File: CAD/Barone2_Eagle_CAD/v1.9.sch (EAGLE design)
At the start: 57 parts, among them J1 USB_C_Port_Raspberry_Pi, J2 XT60-M, J3 10033854-052FSLF, M1 PIC32MX340F512H-80I/MR, M2 RaspberryPi_DDR2_SODIMM_1.8V, Q2 BSS138

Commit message: wiring up board
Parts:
- removed 2V8_OUT: STMICROELECTRONICS_LD1117DT33CTRSTMICROELECTRONICS_LD1117DT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, STMicroelectronics - LD1117DT33CTR:STMICROELECTRONICS_LD1117DT33CTRSTMICROELECTRONICS_LD1117DT33CTR_0_2
- removed C10: 0.1uF, rcl:C-USC0805
- removed C8: 10uF, rcl:C-USC0805
- removed J3: 10033854-052FSLF, 10033854-052FSLF:10033854-052FSLF
- removed M2: RaspberryPi_DDR2_SODIMM_1.8V, con-amp:1376408-SLOT_1.8V
- added 1V8_OUT1: STMICROELECTRONICS_LD1117DT33CTRSTMICROELECTRONICS_LD1117DT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, STMicroelectronics - LD1117DT33CTR:STMICROELECTRONICS_LD1117DT33CTRSTMICROELECTRONICS_LD1117DT33CTR_0_2
- added C20: 10uF, rcl:C-USC0805
- added C21: 0.1uF, rcl:C-USC0805
- added C22: 0.01uF, rcl:C-USC0805
- added JP1: (no value), adafruit:PINHD-1X8CLEANBIG
- added Q1, SCL_OUT_IMU1: BSS138, BSS138:BSS138
- added SODIMM_M2_PINOUT: 10033854-052FSLF, 10033854-052FSLF:10033854-052FSLF
- added X1: CB3LV-3C-8M0000, CB3LV-3C-20M0000:CB3LV-3C-20M0000
- added Y1: ABRACON_ASEK-32_768KHZ-LRTABRACON_ASEK-32_768KHZ-LRT_0_0, Abracon - ASEK-32.768KHZ-LRT:ABRACON_ASEK-32_768KHZ-LRTABRACON_ASEK-32_768KHZ-LRT_0_0
- SON_0: SPICEPREFIX (none) -> X
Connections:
- net +5V renamed 5V
- net N$1 renamed VCAP_VCORE_M1
- removed net 2.8V: 2V8_OUT.VOUT, C8.1
- removed net D+_M2: J1.D-, M2-167.1
- removed net D-_M2: J1.D+, M2-165.1
- removed net M2_1V8: M2-183.1, M2-184.1, M2-185.1, M2-186.1
- removed net M2_VBAT: M2-197.1, M2-198.1, M2-199.1, M2-200.1
- removed net MISO_M1: M1.AN4/C1IN-/CN6/RB4, M2-29.1, R1.2, U$6.DATA_OUT
- removed net MOSI_M1: M1.AN5/C1IN+/CN7/RB5, M2-33.1, R11.2, U$6.DATA_IN
- removed net N$15: M2-41.1, M2-42.1
- removed net SCK_M1: M1.AN3/C2IN+/CN5/RB3, M2-35.1, R12.2, U$6.SCLK
- new net AVDD3_M1: C16.2, M1.VDD3
- new net AVDD_M1: C5.2, M1.AVDD
- new net AVSS_M1: C5.1, M1.AVSS
- new net GPIO13_M2: JP1.8, SODIMM_M2_PINOUTG$1.47
- new net GPIO14_M2: JP1.7, SODIMM_M2_PINOUTG$1.51
- new net GPIO15_M2: JP1.6, SODIMM_M2_PINOUTG$1.53
- new net GPIO16_M2: JP1.5, SODIMM_M2_PINOUTG$1.57
- new net GPIO17_M2: JP1.4, SODIMM_M2_PINOUTG$1.59
- new net GPIO18_M2: JP1.3, SODIMM_M2_PINOUTG$1.63
- new net GPIO19_M2: JP1.2, SODIMM_M2_PINOUTG$1.65
- new net GPIO20_M2: JP1.1, SODIMM_M2_PINOUTG$1.69
- new net IMU_SDA: IMU.SDA/SDI, Q1.D, SCL_OUT_IMU1.G
- new net MISO_M2: M1.AN4/C1IN-/CN6/RB4, R1.2, SODIMM_M2_PINOUTG$1.29, U$6.DATA_OUT
- new net MOSI_M2: M1.AN5/C1IN+/CN7/RB5, R11.2, SODIMM_M2_PINOUTG$1.33, U$6.DATA_IN
- new net N$1: GPS.VCC
- new net N$4: R7.2
- new net N$6: M1.OSC2/CLKO/RC15, X1.EOH
- new net N$7: M1.OSC1/CLKI/RC12, X1.OUT
- new net N$8: M1.SOSCO/T1CK/CN0/RC14, Y1.TRI-STATE
- new net SCK_M2: M1.AN3/C2IN+/CN5/RB3, R12.2, SODIMM_M2_PINOUTG$1.35, U$6.SCLK
- new net USB_D+_M2: J1.D+, SODIMM_M2_PINOUTG$2.165
- new net USB_D-_M2: J1.D-, SODIMM_M2_PINOUTG$2.167
- new net VDD1_M1: C17.2, M1.VDD1
- new net VSS1_M1: C17.1, M1.VSS1
- new net VSS3_M1: C16.1, M1.VSS3
- net 1.8V: now also 1V8_OUT1.VOUT, C14.1, C20.1, IMU.VDD, IMU.VDDIO, Q1.S, Q2.S, SODIMM_M2_PINOUTG$2.183, SODIMM_M2_PINOUTG$2.184, SODIMM_M2_PINOUTG$2.185, SODIMM_M2_PINOUTG$2.186
- net 9.6V-12.6V: no longer 1V8_OUT.VIN, 2V8_OUT.VIN, 5V_OUT.VIN, C10.1, C4.1, C9.1
- net CS_M1: now also SODIMM_M2_PINOUTG$1.4, SODIMM_M2_PINOUTG$1.5; no longer J3G$1.5, M2-5.1
- net CS_MICRO_SD: now also SODIMM_M2_PINOUTG$1.2; no longer J3G$1.2, M2-3.1
- net GND: now also 1V8_OUT1.GND, C20.2, C21.2, C22.2, SODIMM_M2_PINOUTG$1.19, SODIMM_M2_PINOUTG$1.20, SODIMM_M2_PINOUTG$1.31, SODIMM_M2_PINOUTG$1.32, SODIMM_M2_PINOUTG$1.37, SODIMM_M2_PINOUTG$1.38, SODIMM_M2_PINOUTG$1.43, SODIMM_M2_PINOUTG$1.44, SODIMM_M2_PINOUTG$1.49, SODIMM_M2_PINOUTG$1.50, SODIMM_M2_PINOUTG$1.55, SODIMM_M2_PINOUTG$1.56, SODIMM_M2_PINOUTG$1.61, SODIMM_M2_PINOUTG$1.62, SODIMM_M2_PINOUTG$1.67, SODIMM_M2_PINOUTG$1.68, SODIMM_M2_PINOUTG$1.7, SODIMM_M2_PINOUTG$1.73, SODIMM_M2_PINOUTG$1.74, SODIMM_M2_PINOUTG$1.79, SODIMM_M2_PINOUTG$1.8, SODIMM_M2_PINOUTG$1.80, SODIMM_M2_PINOUTG$1.85, SODIMM_M2_PINOUTG$1.86, SODIMM_M2_PINOUTG$1.91, SODIMM_M2_PINOUTG$1.92, SODIMM_M2_PINOUTG$1.97, SODIMM_M2_PINOUTG$1.98, SODIMM_M2_PINOUTG$1.SHIELD, SODIMM_M2_PINOUTG$2.103, SODIMM_M2_PINOUTG$2.104, SODIMM_M2_PINOUTG$2.109, SODIMM_M2_PINOUTG$2.110, SODIMM_M2_PINOUTG$2.115, SODIMM_M2_PINOUTG$2.116, SODIMM_M2_PINOUTG$2.121, SODIMM_M2_PINOUTG$2.122, SODIMM_M2_PINOUTG$2.127, SODIMM_M2_PINOUTG$2.133, SODIMM_M2_PINOUTG$2.134, SODIMM_M2_PINOUTG$2.139, SODIMM_M2_PINOUTG$2.140, SODIMM_M2_PINOUTG$2.145, SODIMM_M2_PINOUTG$2.146, SODIMM_M2_PINOUTG$2.151, SODIMM_M2_PINOUTG$2.152, SODIMM_M2_PINOUTG$2.157, SODIMM_M2_PINOUTG$2.163, SODIMM_M2_PINOUTG$2.164, SODIMM_M2_PINOUTG$2.168, SODIMM_M2_PINOUTG$2.169, SODIMM_M2_PINOUTG$2.170, SODIMM_M2_PINOUTG$2.181, SODIMM_M2_PINOUTG$2.182, SODIMM_M2_PINOUTG$2.187, SODIMM_M2_PINOUTG$2.188, SODIMM_M2_PINOUTG$2.195, SODIMM_M2_PINOUTG$2.196, X1.GND, Y1.GND; no longer 2V8_OUT.GND, C10.2, C16.1, C17.1, C5.1, C8.2, J3G$1.7, J3G$1.8, M1.AVSS, M1.VSS1, M1.VSS3, M2-1.1, M2-103.1, M2-104.1, M2-109.1, M2-110.1, M2-115.1, M2-116.1, M2-121.1, M2-122.1, M2-127.1, M2-13.1, M2-133.1, M2-134.1, M2-139.1, M2-14.1, M2-140.1, M2-145.1, M2-146.1, M2-151.1, M2-152.1, M2-157.1, M2-163.1, M2-164.1, M2-168.1, M2-169.1, M2-170.1, M2-181.1, M2-182.1, M2-187.1, M2-188.1, M2-19.1, M2-195.1, M2-196.1, M2-20.1, M2-25.1, M2-26.1, M2-31.1, M2-32.1, M2-37.1, M2-38.1, M2-43.1, M2-44.1, M2-49.1, M2-50.1, M2-55.1, M2-56.1, M2-61.1, M2-62.1, M2-67.1, M2-68.1, M2-7.1, M2-73.1, M2-74.1, M2-79.1, M2-8.1, M2-80.1, M2-85.1, M2-86.1, M2-91.1, M2-92.1, M2-97.1, M2-98.1
- net GPIO12_M2: now also SODIMM_M2_PINOUTG$1.45; no longer M2-45.1
- net GPIO2_M2: now also SODIMM_M2_PINOUTG$1.9; no longer M2-9.1
- net GPIO3_M2: now also SODIMM_M2_PINOUTG$1.11; no longer M2-11.1
- net GPIO4_M2: now also SODIMM_M2_PINOUTG$1.15; no longer M2-15.1
- net GPIO5_M2: now also SODIMM_M2_PINOUTG$1.17; no longer M2-17.1
- net GPIO6_M2: now also SODIMM_M2_PINOUTG$1.21; no longer M2-21.1
- net GPIO7_M2: now also SODIMM_M2_PINOUTG$1.23; no longer M2-23.1
- net GPIO8_M2: now also SODIMM_M2_PINOUTG$1.27; no longer M2-27.1
- net N$9: now also M1.SOSCI/CN1/RC13, Y1.OUTPUT; no longer M2-39.1, M2-40.1
- net SDA_M1: now also Q1.G, SCL_OUT_IMU1.D; no longer IMU.SDA/SDI
- net VIN: now also 1V8_OUT.VIN, 1V8_OUT1.VIN, 5V_OUT.VIN, C21.1, C22.1, C4.1, C9.1, SCL_OUT_IMU1.S, SODIMM_M2_PINOUTG$1.39, SODIMM_M2_PINOUTG$1.40, SODIMM_M2_PINOUTG$1.41, SODIMM_M2_PINOUTG$1.42, SODIMM_M2_PINOUTG$2.189, SODIMM_M2_PINOUTG$2.190, SODIMM_M2_PINOUTG$2.191, SODIMM_M2_PINOUTG$2.192, SODIMM_M2_PINOUTG$2.193, SODIMM_M2_PINOUTG$2.194, SODIMM_M2_PINOUTG$2.197, SODIMM_M2_PINOUTG$2.198, SODIMM_M2_PINOUTG$2.199, SODIMM_M2_PINOUTG$2.200, X1.VCC, Y1.VDD; no longer C14.1, C16.2, C17.2, C5.2, GPS.VCC, IMU.VDD, IMU.VDDIO, M1.AVDD, M1.VDD1, M1.VDD3, M2-189.1, M2-190.1, M2-191.1, M2-193.1, Q2.S, R7.2
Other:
- note added: "(PIN168)USB_OTGID connected to GND when unused"
- note removed: "5.0V-5.2V to 1.8V voltage regulator"
- note removed: "5.0V-5.2V to 2.8V voltage regulator"
- note removed: "5.0V-5.2V to 5V voltage regulator"
- note removed: "Powers GPIO 0-27 pins"
- note removed: "Powers GPIO 28-45 pins"
- note removed: "Powers PHYs, IO and SDRAM"
- note removed: "Powers composite (TV-out) DAC"
- note removed: "USB_OnTheGo Pin 168 Unused"
- moved on the sheet: 1V8_OUT, 3V3_OUT, 5V_OUT, B1, C1, C11, C12, C13, C14, C15, C16, C17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

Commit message: Added ballon pressure sensor, oscillators, logic level convers
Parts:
- removed 1V8_OUT1: STMICROELECTRONICS_LD1117DT33CTRSTMICROELECTRONICS_LD1117DT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, STMicroelectronics - LD1117DT33CTR:STMICROELECTRONICS_LD1117DT33CTRSTMICROELECTRONICS_LD1117DT33CTR_0_2
- removed D4: (no value), adafruit:DIODESOD-323F
- added 1V8_M2, 5V_M2, 5V_SRVO_0, 5V_SRVO_1, 5V_SRVO_2, 5V_SRVO_3: STMICROELECTRONICS_LD1117DT33CTRSTMICROELECTRONICS_LD1117DT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, STMicroelectronics - LD1117DT33CTR:STMICROELECTRONICS_LD1117DT33CTRSTMICROELECTRONICS_LD1117DT33CTR_0_2
- added 5V, GND: 1X4-BIG, adafruit:1X4-BIG
- added C10, C26, C27, C29, C31: 0.1uF, rcl:C-USC0805
- added C24, C25, C28, C30, C8: 10uF, rcl:C-USC0805
- added R2, R3: 10k, adafruit:R-US_R0805W
- renumbered 5V_OUT to 5V_SON
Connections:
- removed net INT_ICM20948: IMU.INT1, M1.!SS2!/PMA2/CN11/RG9
- new net 5V1: 5V.1, 5V_SRVO_3.VOUT, C30.1
- new net CSN_IMU: 1V8_OUT.VOUT, C14.1, C6.1, IMU.!CS, IMU.VDD, IMU.VDDIO, Q1.S, Q2.S
- new net INT_IMU: IMU.INT1, M1.SDI2/PMA4/CN9/RG7
- new net N$11: 5V_SON.VIN, C4.1
- new net N$12: 5V_M2.VIN, 5V_SRVO_0.VIN, C10.1, C26.1
- new net N$15: 5V.2, 5V_SRVO_2.VOUT, C28.1
- new net N$16: 5V_SRVO_3.VIN, C31.1
- net 1.8V: now also 1V8_M2.VOUT; no longer 1V8_OUT.VOUT, 1V8_OUT1.VOUT, C14.1, C6.1, IMU.VDD, IMU.VDDIO, Q1.S, Q2.S
- net 5V: now also 5V.4, 5V_M2.VOUT, 5V_SRVO_0.VOUT, C25.1, C8.1, SODIMM_M2_PINOUTG$2.197, SODIMM_M2_PINOUTG$2.198, SODIMM_M2_PINOUTG$2.199, SODIMM_M2_PINOUTG$2.200
- net GND: now also 1V8_M2.GND, 5V_M2.GND, 5V_SRVO_0.GND, 5V_SRVO_1.GND, 5V_SRVO_2.GND, 5V_SRVO_3.GND, C10.2, C24.2, C25.2, C26.2, C27.2, C28.2, C29.2, C30.2, C31.2, C8.2, GND.1, GND.2, GND.3, GND.4; no longer 1V8_OUT1.GND, IMU.RESV_20
- net INT1_MPL3115: now also M1.PGED1/AN0/VREF+/CVREF+/PMA6/CN2/RB0; no longer M1.SDI2/PMA4/CN9/RG7
- net INT2_MPL3115: now also M1.PGEC1/AN1/VREF-/CVREF-/CN3/RB1; no longer M1.SDO2/PMA3/CN10/RG8
- net N$21: now also B1.+; no longer D4.C
- net N$5: now also 5V.3, 5V_SRVO_1.VOUT, C24.1; no longer B1.+, D4.A
- net SCL_M1: now also R3.1
- net SDA_M1: now also R2.1
- net VIN: now also 1V8_M2.VIN, 5V_SRVO_1.VIN, 5V_SRVO_2.VIN, C27.1, C29.1, R2.2, R3.2; no longer 1V8_OUT1.VIN, 5V_SON.VIN, C4.1, IMU.!CS, SODIMM_M2_PINOUTG$2.197, SODIMM_M2_PINOUTG$2.198, SODIMM_M2_PINOUTG$2.199, SODIMM_M2_PINOUTG$2.200
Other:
- note added: "Power to 4 sevos"
- moved on the sheet: C20, C21, R4, SON_0

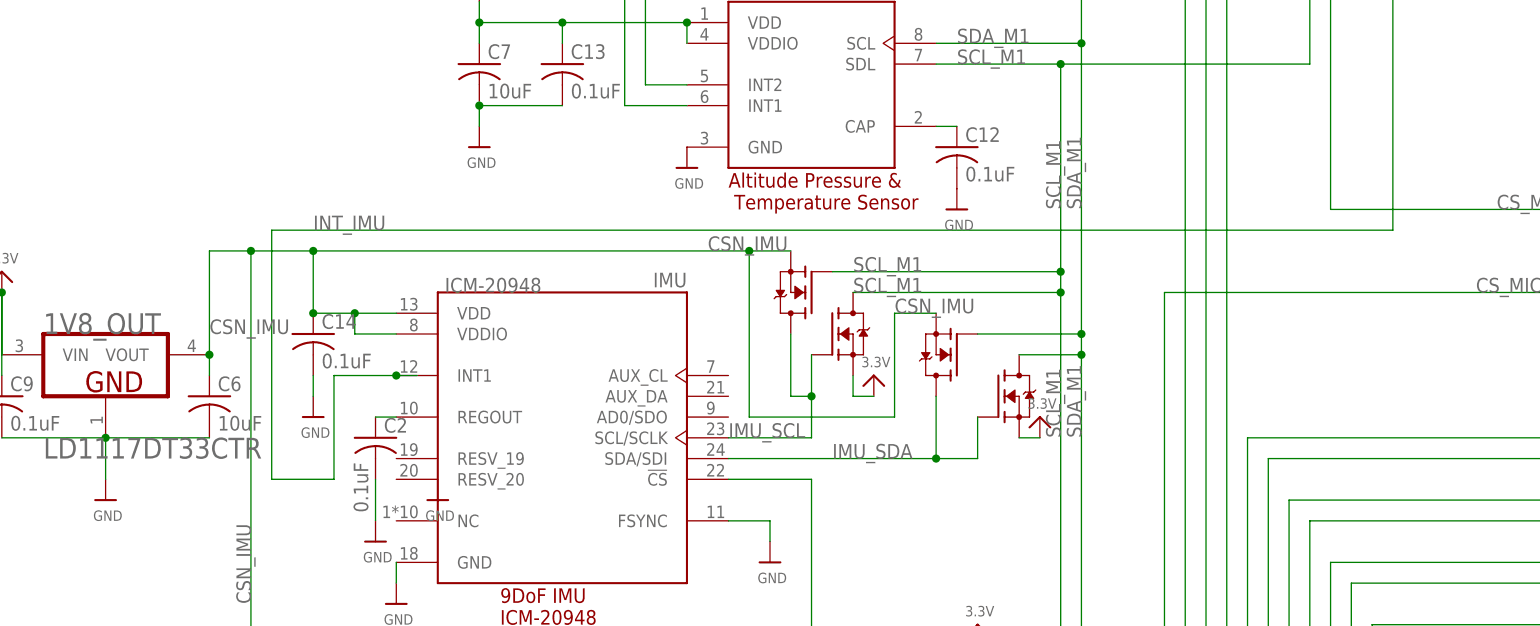
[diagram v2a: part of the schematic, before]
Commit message: added logic level converter for interupt pin of IMU
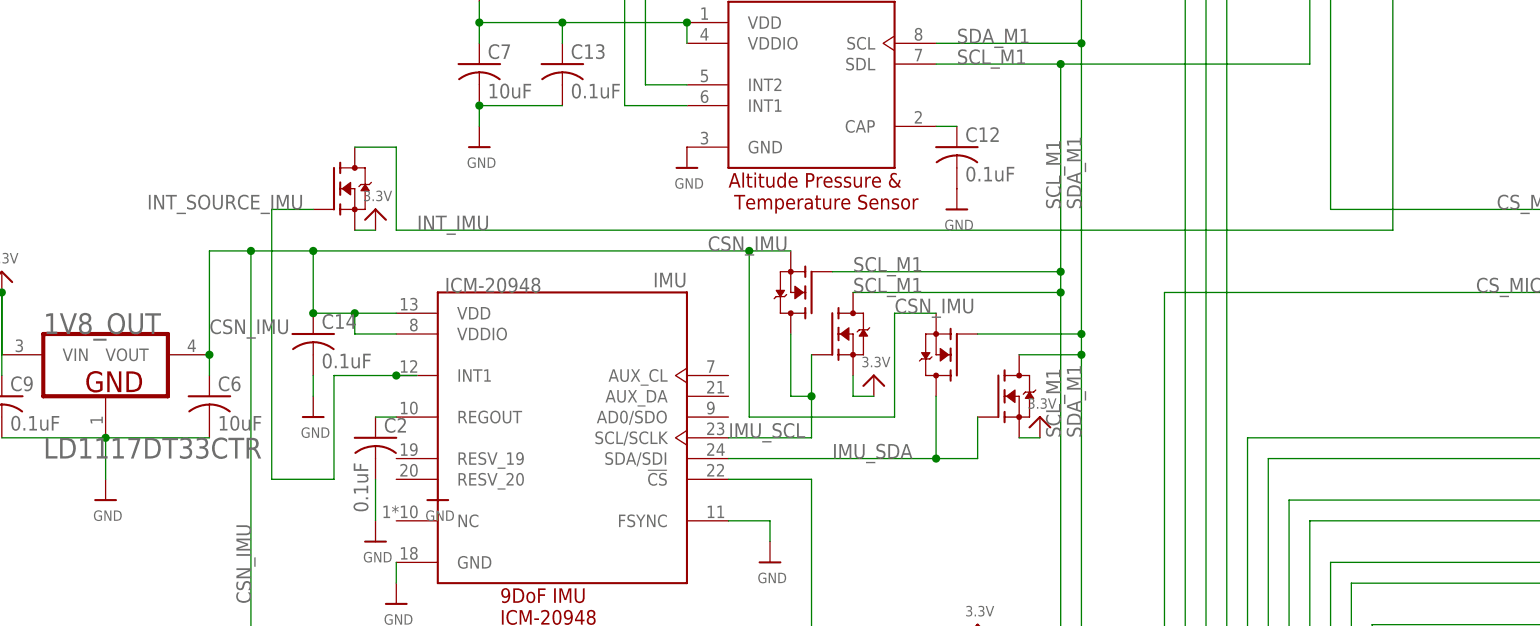
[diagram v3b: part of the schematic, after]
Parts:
- added INT_LLC_IMU: BSS138, BSS138:BSS138
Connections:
- new net INT_SOURCE_IMU: IMU.INT1, INT_LLC_IMU.G
- net INT_IMU: now also INT_LLC_IMU.D; no longer IMU.INT1
- net VIN: now also INT_LLC_IMU.S
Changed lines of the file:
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@@
 <part name="U$54" library="microbuilder" deviceset="GND" device=""/>
 <part name="U$55" library="microbuilder" deviceset="VIN" device="" value="11.1V"/>
+<part name="INT_LLC_IMU" library="BSS138" deviceset="BSS138" device=""/>
+<part name="U$25" library="microbuilder" deviceset="VIN" device="" value="3.3V"/>
 </parts>
 <sheets>
@@
 <attribute name="VALUE" x="430.276" y="354.076" size="1.27" layer="96"/>
 </instance>
+<instance part="INT_LLC_IMU" gate="G$1" x="53.34" y="208.28" smashed="yes"/>
+<instance part="U$25" gate="G$1" x="58.42" y="205.74" smashed="yes">
+<attribute name="VALUE" x="56.896" y="206.756" size="1.27" layer="96"/>
+</instance>
 </instances>
 <busses>
@@
 <junction x="396.24" y="332.74"/>
 </segment>
+<segment>
+<pinref part="INT_LLC_IMU" gate="G$1" pin="S"/>
+<pinref part="U$25" gate="G$1" pin="VIN"/>
+<wire x1="55.88" y1="203.2" x2="58.42" y2="203.2" width="0.1524" layer="91"/>
+</segment>
 </net>
 <net name="ECHO_SON0" class="0">
@@
 <net name="INT_IMU" class="0">
 <segment>
-<pinref part="IMU" gate="G$1" pin="INT1"/>
-<wire x1="60.96" y1="185.42" x2="63.5" y2="185.42" width="0.1524" layer="91"/>
-<label x="50.8" y="203.2" size="1.778" layer="95"/>
-<wire x1="60.96" y1="185.42" x2="53.34" y2="185.42" width="0.1524" layer="91"/>
-<junction x="60.96" y="185.42"/>
-<wire x1="53.34" y1="185.42" x2="53.34" y2="172.72" width="0.1524" layer="91"/>
-<wire x1="53.34" y1="172.72" x2="45.72" y2="172.72" width="0.1524" layer="91"/>
-<wire x1="45.72" y1="172.72" x2="45.72" y2="203.2" width="0.1524" layer="91"/>
-<wire x1="45.72" y1="203.2" x2="182.88" y2="203.2" width="0.1524" layer="91"/>
 <pinref part="M1" gate="G$1" pin="SDI2/PMA4/CN9/RG7"/>
 <wire x1="193.04" y1="297.18" x2="182.88" y2="297.18" width="0.1524" layer="91"/>
 <wire x1="182.88" y1="297.18" x2="182.88" y2="203.2" width="0.1524" layer="91"/>
 <label x="182.88" y="297.18" size="1.778" layer="95"/>
+<pinref part="INT_LLC_IMU" gate="G$1" pin="D"/>
+<wire x1="55.88" y1="213.36" x2="60.96" y2="213.36" width="0.1524" layer="91"/>
+<wire x1="60.96" y1="213.36" x2="60.96" y2="203.2" width="0.1524" layer="91"/>
+<wire x1="60.96" y1="203.2" x2="182.88" y2="203.2" width="0.1524" layer="91"/>
+<label x="63.5" y="203.2" size="1.778" layer="95"/>
 </segment>
 </net>
@@
 </segment>
 </net>
+<net name="INT_SOURCE_IMU" class="0">
+<segment>
+<pinref part="IMU" gate="G$1" pin="INT1"/>
+<wire x1="60.96" y1="185.42" x2="63.5" y2="185.42" width="0.1524" layer="91"/>
+<junction x="60.96" y="185.42"/>
+<wire x1="60.96" y1="185.42" x2="53.34" y2="185.42" width="0.1524" layer="91"/>
+<wire x1="53.34" y1="185.42" x2="53.34" y2="172.72" width="0.1524" layer="91"/>
+<wire x1="53.34" y1="172.72" x2="45.72" y2="172.72" width="0.1524" layer="91"/>
+<wire x1="45.72" y1="172.72" x2="45.72" y2="205.74" width="0.1524" layer="91"/>
+<pinref part="INT_LLC_IMU" gate="G$1" pin="G"/>
+<wire x1="45.72" y1="205.74" x2="50.8" y2="205.74" width="0.1524" layer="91"/>
+<label x="30.48" y="205.74" size="1.778" layer="95"/>
+</segment>
+</net>

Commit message: Added Transmitter pinout
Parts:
- removed 5V: 1X4-BIG, adafruit:1X4-BIG
- removed 5V_SRVO_0, 5V_SRVO_1, 5V_SRVO_2, 5V_SRVO_3: STMICROELECTRONICS_LD1117DT33CTRSTMICROELECTRONICS_LD1117DT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, STMicroelectronics - LD1117DT33CTR:STMICROELECTRONICS_LD1117DT33CTRSTMICROELECTRONICS_LD1117DT33CTR_0_2
- removed C24, C25, C28, C30: 10uF, rcl:C-USC0805
- removed C26, C27, C29, C31: 0.1uF, rcl:C-USC0805
- added 5V_BUCK_IN, CAMERA_POWER, RC_RECEIVER_POWER, UART_M0: 1X2-3.5MM, adafruit:1X2-3.5MM
- added 5V_BUCK_OUT: 1X4-BIG, adafruit:1X4-BIG
- added J3: USB_C_Port_PIC32, DX07S016JA1R1500:DX07S016JA1R1500
- added R5: 47k, adafruit:R-US_R0805W
- added U1: FT232RQ, FT232RQ:FT232RQ
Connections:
- removed net 5V1: 5V.1, 5V_SRVO_3.VOUT, C30.1
- new net N$14: R5.2, RC_RECEIVER_POWER.1
- new net RXD0_M2: SODIMM_M2_PINOUTG$1.60, UART_M0.2
- new net TXD0_M2: SODIMM_M2_PINOUTG$1.58, UART_M0.1
- new net U2RX_M1: M1.SDA2/U2RX/PMA9/CN17/RF4, U1.TXD
- new net U2TX_M1: M1.SCL2/U2TX/PMA8/CN18/RF5, U1.RXD
- net 5V: now also U1.VCC; no longer 5V.4, 5V_SRVO_0.VOUT, C25.1
- net 9.6V-12.6V: now also CAMERA_POWER.1, R5.1
- net GND: now also 5V_BUCK_IN.2, CAMERA_POWER.2, J3.GND, J3.SHIELD, RC_RECEIVER_POWER.2, U1.AGND, U1.GND, U1.TEST; no longer 5V_SRVO_0.GND, 5V_SRVO_1.GND, 5V_SRVO_2.GND, 5V_SRVO_3.GND, C24.2, C25.2, C26.2, C27.2, C28.2, C29.2, C30.2, C31.2
- net N$12: no longer 5V_SRVO_0.VIN, C26.1
- net N$15: now also J3.D-, U1.USBDM; no longer 5V.2, 5V_SRVO_2.VOUT, C28.1
- net N$16: now also J3.D+, U1.USBDP; no longer 5V_SRVO_3.VIN, C31.1
- net N$5: now also 5V_BUCK_IN.1, 5V_BUCK_OUT.1, 5V_BUCK_OUT.2, 5V_BUCK_OUT.3, 5V_BUCK_OUT.4; no longer 5V.3, 5V_SRVO_1.VOUT, C24.1
- net VIN: now also U1.VCCIO; no longer 5V_SRVO_1.VIN, 5V_SRVO_2.VIN, C27.1, C29.1
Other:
- note added: "Power to camera transmitter"
- note added: "Power to receiver"
- note added: "RX: GPIO2_M2 Throttle SHALL GPIO3_M2 Turn (Rudder) SHALL GPIO4_M2 Forward (Elevator) SHALL GPIO5_M2 Aileron (No connect) SHALL GPIO6_M2 Autonomous/RC SHALL GPIO7_M2 Autoland SHOULD GPIO8_M2 Ascend/Descend BTN SHALL TX: Battery percentage SHALL Error Status SHALL GPS SHALL Magnetometer data SHOULD"
- moved on the sheet: 1V8_M2, 3V3_OUT, 5V_M2, C10, C18, C19, C20, C21, C8, GND, J1, J2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

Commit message: Fixing ECE121 source code
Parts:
- renumbered Q1 to SDA_OUT_IMU
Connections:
- removed net CSN_IMU: 1V8_OUT.VOUT, C14.1, C6.1, IMU.!CS, IMU.VDD, IMU.VDDIO, Q2.S, SDA_OUT_IMU.S
- removed net N$11: 5V_SON.VIN, C4.1
- removed net N$12: 5V_M2.VIN, C10.1
- net 1.8V: now also 1V8_OUT.VOUT, C14.1, C6.1, IMU.!CS, IMU.VDD, IMU.VDDIO, Q2.S, SDA_OUT_IMU.S
- net 9.6V-12.6V: now also 5V_M2.VIN, 5V_SON.VIN, C10.1, C4.1

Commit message: 60% complete with board wiring
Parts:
- PIC32_USB: value USB_C_Port_PIC32 -> DX07S016JA1R1500
- RASPBERRY_PI_USB: value USB_C_Port_Raspberry_Pi -> DX07S016JA1R1500
- renumbered J1 to RASPBERRY_PI_USB, J3 to PIC32_USB
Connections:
- removed net N$4: R7.2
- net CS_M1: no longer SODIMM_M2_PINOUTG$1.4
- net VIN: now also R7.2

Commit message: Fixed GND and 3.3V via issues, currently validating DRC errors
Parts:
- removed R15: 470, adafruit:R-US_R0805W
- removed R16: 10k, adafruit:R-US_R0805W
- removed U$6: MICROSD, adafruit:MICROSD
- added EMMC_DISABLE_N, ESC_POWER: 1X2-3.5MM, adafruit:1X2-3.5MM
- added R6: 10k, adafruit:R-US_R0805W
- R1: value 47k -> 470
- R11, R5: value 47k -> 10k
- R13: value 10k -> 47k
- R2: value 10k -> 680
- renumbered Q2 to SCL_IN_IMU, SCL_OUT_IMU1 to SDA_IN_IMU1, UART_M0 to UART_M2
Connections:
- removed net 3.3V: 3V3_OUT.VOUT, C18.1
- removed net CS_MICRO_SD: R14.2, SODIMM_M2_PINOUTG$1.2, U$6.CS
- removed net GND1: U$6.GND, U$6.GND1
- removed net VDD: U$6.VDD
- removed net VSS: U$6.VSS
- new net N$4: EMMC_DISABLE_N.1, SODIMM_M2_PINOUTG$1.2
- net 9.6V-12.6V: now also ESC_POWER.1, R2.1; no longer R5.1
- net CS_M1: no longer SODIMM_M2_PINOUTG$1.5
- net ECHO_SON0: now also R3.2; no longer R4.2
- net ECHO_SON1: now also R4.2; no longer R9.2
- net ECHO_SON2: now also R5.2; no longer R10.2
- net ECHO_SON3: now also R6.2; no longer R13.2
- net GND: now also EMMC_DISABLE_N.2, ESC_POWER.2, R3.1, R5.1, R6.1; no longer R10.1, R13.1, R9.1
- net MCLR_M1: now also R1.2, R11.2; no longer R15.2, R16.2
- net MISO_M2: now also R12.2; no longer R1.2, U$6.DATA_OUT
- net MOSI_M2: now also R13.2; no longer R11.2, U$6.DATA_IN
- net N$13: now also R1.1; no longer R15.1
- net N$14: now also R2.2; no longer R5.2
- net SCK_M2: now also R14.2; no longer R12.2, U$6.SCLK
- net SCL_M1: now also MPL3115.SCL, R8.1; no longer MPL3115.SDL, R3.1
- net SDA_M1: now also MPL3115.SDL, R7.1; no longer MPL3115.SCL, R2.1
- net U1RX_M1: now also R9.1; no longer R7.1
- net U1TX_M1: now also R10.1; no longer R8.1
- net VIN: now also 3V3_OUT.VOUT, C18.1, R10.2, R13.1, R9.2; no longer R1.1, R16.1, R2.2, R3.2
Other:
- note added: "Data telemetry UART to transmitter"
- note added: "EMMC DISABLE N jumper (connected both pins to disable microprocessor from reading eMMC memory)"
- note added: "Power input from buck converter"
- note added: "Power to ESC"
- moved on the sheet: R1, R10, R11, R12, R13, R14, R2, R3, R4, R5, R7, R8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

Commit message: Added GND to A0 pin of ICM-20948 IMU sensor, removed one 1.8V and 5.0V voltage regulators.
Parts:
- removed 1V8_M2, 5V_M2: STMICROELECTRONICS_LD1117DT33CTRSTMICROELECTRONICS_LD1117DT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, STMicroelectronics - LD1117DT33CTR:STMICROELECTRONICS_LD1117DT33CTRSTMICROELECTRONICS_LD1117DT33CTR_0_2
- removed C10, C21: 0.1uF, rcl:C-USC0805
- removed C20, C8: 10uF, rcl:C-USC0805
- added UART_M2_TX_POWER: 1X2-3.5MM, adafruit:1X2-3.5MM
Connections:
- removed net N$1: GPS.VCC
- net 1.8V: no longer 1V8_M2.VOUT, C20.1
- net 5V: now also UART_M2_TX_POWER.1; no longer 5V_M2.VOUT, C8.1
- net 9.6V-12.6V: no longer 5V_M2.VIN, C10.1
- net GND: now also IMU.AD0/SDO, UART_M2_TX_POWER.2; no longer 1V8_M2.GND, 5V_M2.GND, C10.2, C20.2, C21.2, C8.2
- net VIN: now also GPS.VCC; no longer 1V8_M2.VIN, C21.1
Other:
- note added: "Power to telemetry transmitter"
